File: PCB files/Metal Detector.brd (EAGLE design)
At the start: 100 x 80 mm, 105 parts, among them IC1 NE5534AD, IC2 BQ24133RGYR, IC4 ESP32-WROOM-32UE-N4, IC6 TLV62130ARGTR, IC7 TLV1117-33IDCYR, J1 DG128-7.5, J2 DG128-7.5, Q1 IRF740, Q11 MMBT3904, Q3 SI2312CDS-T1-GE3, Q5 SI2312CDS-T1-GE3, Q6 SI2323CDS-T1-GE3, Q9 MMBT3904, X2 DC21MMX

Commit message: Add files via upload
Started design PCB layout first start from battery charge circut, still desing process
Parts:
- removed Q5: SI2312CDS-T1-GE3, SI2312CDS-T1-GE3:SOT95P237X112-3N
- removed Q6: SI2323CDS-T1-GE3, SI2323CDS-T1-GE3:SOT95P237X112-3N
- removed R30: 0.02RΩ, rcl:R1206
- removed R31: 0RΩ, rcl:R1206
- removed R33: 0.01RΩ, rcl:R1206
- added Q2, Q4: IRF740, IRF740:TO220BV
- added R14: 0.02Ω, rcl:R2010
- added R19: 0.01Ω, rcl:R2010
- added R21: 0Ω, rcl:R0603
- Q3: value SI2312CDS-T1-GE3 -> IRF9630; device SI2312CDS-T1-GE3:SOT95P237X112-3N -> IRF9630:TO254P465X1024X2050-3P
- moved BATTERYPIN 1425.9 mm to (6.35, 58.4), turned to 270 degrees
- moved R49 1362.9 mm to (44.5, 58.4), turned to 270 degrees
- moved R43 671.6 mm to (57.1, 55.9)
- moved R42 670.4 mm to (57.1, 59.7), turned to 180 degrees
- moved R41 666.6 mm to (48.3, 63.5)
- moved C37 665.2 mm to (34.3, 77.5), turned to 180 degrees
- moved C38 662.8 mm to (52.1, 63.5)
- moved C35 639.0 mm to (63.5, 92.7), turned to 90 degrees
- moved R40 625.3 mm to (57.1, 48.3)
- moved R39 621.0 mm to (47.0, 52.1)
- moved R38 617.7 mm to (52.1, 52.1)
- moved R37 607.7 mm to (47.0, 48.3)
- moved R35 607.3 mm to (62.2, 64.8)
- moved R36 604.4 mm to (52.1, 48.3)
- moved C34 603.8 mm to (66.0, 64.8), turned to 180 degrees
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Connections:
- net 12V_IN: now also Q2.D; no longer Q3.3
- net ACN: now also R21.2; no longer R31.1
- net ACP: now also Q4.D, R14.1; no longer Q5.3, R30.1
- net GND: now also BATTERYPIN.2, BATTERYPIN.4; no longer BATTERYPIN.1, BATTERYPIN.3
- net N$21: now also Q2.S, Q4.S; no longer Q3.2, Q5.2
- net N$22: now also Q2.G, Q4.G; no longer Q3.1, Q5.1
- net N$23: now also Q3.1; no longer Q6.1
- net SRP: now also R19.1; no longer R33.1
- net TS: now also BATTERYPIN.3; no longer BATTERYPIN.2
- net VBATT: now also BATTERYPIN.1, Q3.2, R19.2; no longer BATTERYPIN.4, Q6.3, R33.2
- net VCCINT: now also Q3.3, R14.2, R21.1; no longer Q6.2, R30.2, R31.2
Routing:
- net VBATT: track 0.00 -> 55.2 mm
- net 12V_IN: track 0.00 -> 37.4 mm
- net N$22: track 0.00 -> 28.0 mm
- net N$21: track 0.00 -> 25.4 mm
- net VCCINT: track 0.00 -> 22.5 mm
- net ACP: track 0.00 -> 22.0 mm, vias 0 -> 1
- net VCC: track 0.00 -> 16.9 mm
- net SRP: track 0.00 -> 10.3 mm
- net OVPSET: track 0.00 -> 8.63 mm
- net ACN: track 0.00 -> 7.05 mm, vias 0 -> 1
- net N$16: track 0.00 -> 6.34 mm
- net N$23: track 0.00 -> 5.50 mm
- net AVCC: track 0.00 -> 5.22 mm
- net CMSRC: track 0.00 -> 4.20 mm, vias 0 -> 1
- net TS: track 0.00 -> 3.81 mm
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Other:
- board size 100 x 80 mm -> 89 x 100.3 mm

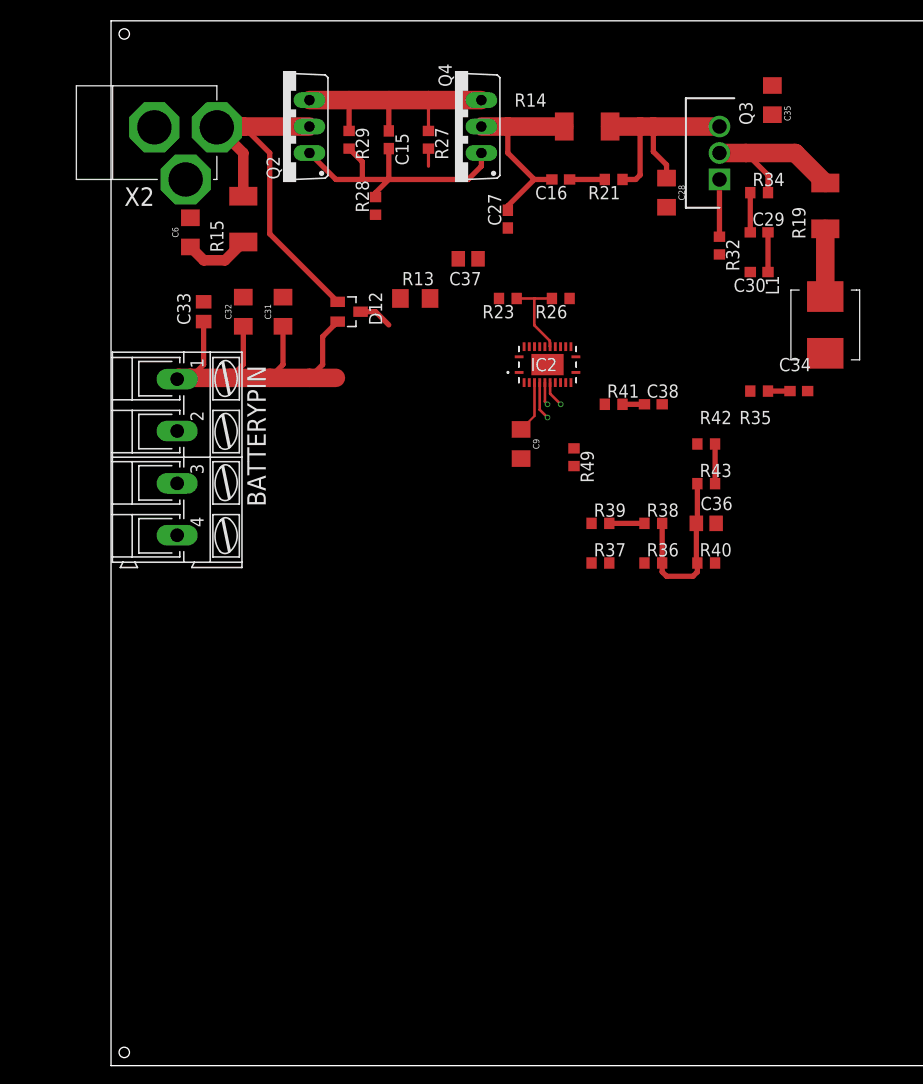
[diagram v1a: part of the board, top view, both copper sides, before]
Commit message: Add files via upload
Battery charge circuit on design progress
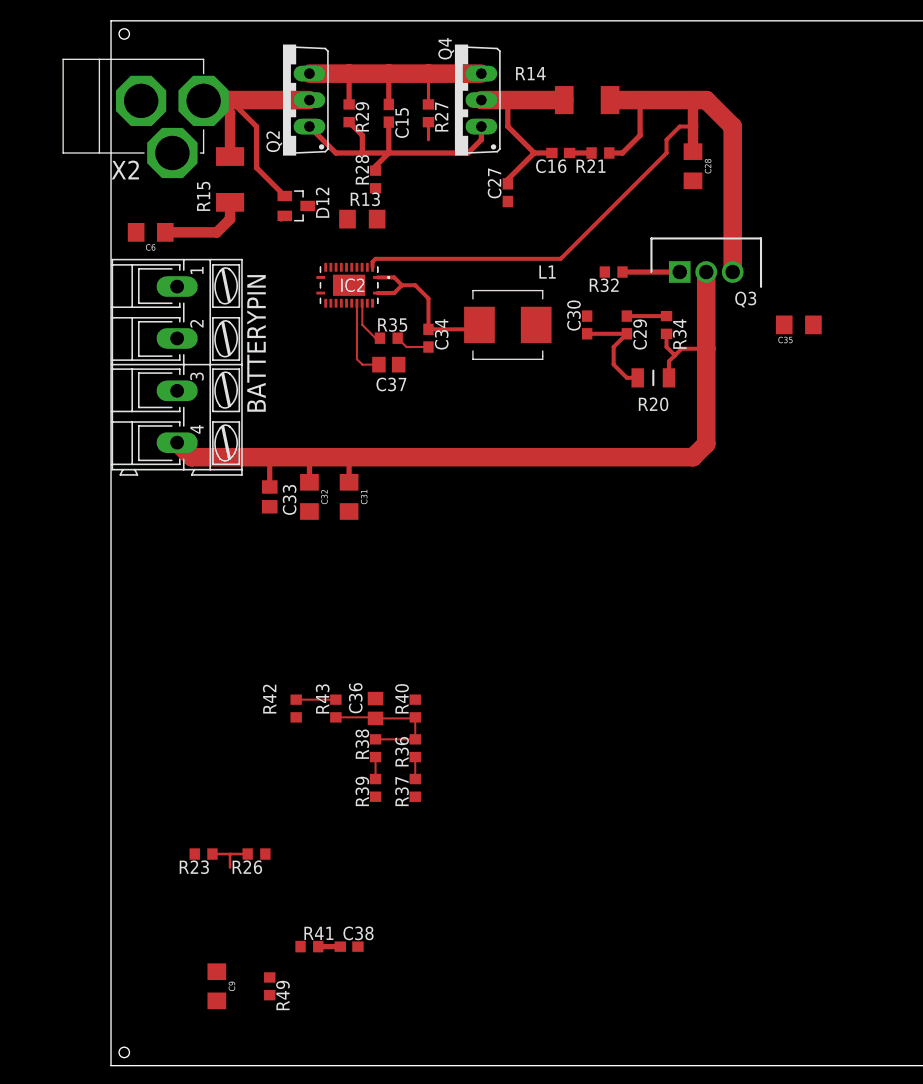
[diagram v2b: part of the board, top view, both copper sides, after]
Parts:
- removed R19: 0.01Ω, rcl:R2010
- added R20: WSL1206R0100FEK18, WSL1206R0100FEK18:RESC3216X89N
- moved R23 60.8 mm to (8.89, 20.3)
- moved R26 60.8 mm to (14.0, 20.3)
- moved C38 59.7 mm to (22.9, 11.4)
- moved C9 59.7 mm to (10.2, 7.62)
- moved R41 59.7 mm to (19.1, 11.4)
- moved R49 58.6 mm to (15.2, 7.62)
- moved R42 46.9 mm to (17.8, 34.3), turned to 270 degrees
- moved R43 41.6 mm to (21.6, 34.3), turned to 90 degrees
- moved C36 36.4 mm to (25.4, 34.3), turned to 270 degrees
- moved C34 35.9 mm to (30.5, 69.8), turned to 270 degrees
- moved R35 35.9 mm to (26.7, 69.8)
- moved R38 34.3 mm to (25.4, 30.5), turned to 90 degrees
- moved R39 33.3 mm to (25.4, 26.7), turned to 90 degrees
- moved R40 31.2 mm to (29.2, 34.3), turned to 90 degrees
- moved L1 30.5 mm to (38.1, 71.1), turned to 0 degrees
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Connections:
- net GND: now also BATTERYPIN.1, BATTERYPIN.3; no longer BATTERYPIN.2, BATTERYPIN.4
- net SRP: now also R20.1; no longer R19.1
- net TS: now also BATTERYPIN.2; no longer BATTERYPIN.3
- net VBATT: now also BATTERYPIN.4, R20.2; no longer BATTERYPIN.1, R19.2
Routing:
- net VCCINT: track 22.5 -> 76.2 mm
- net VBATT: track 55.2 -> 84.6 mm
- net SW: track 0.00 -> 16.4 mm
- net 12V_IN: track 37.4 -> 28.9 mm
- net REGN: track 0.00 -> 7.70 mm
- net AVCC: track 5.22 -> 0.19 mm
- net ACN: track 7.05 -> 2.11 mm, vias 1 -> 0
- net BTST: track 0.00 -> 4.31 mm
- net OVPSET: track 8.63 -> 4.68 mm
- net VCC: track 16.9 -> 13.6 mm
- net N$14: track 3.24 -> 0.00 mm
- net CMSRC: track 4.20 -> 1.69 mm, vias 1 -> 0
- net ACP: track 22.0 -> 19.8 mm, vias 1 -> 0
- net N$16: track 6.34 -> 8.49 mm
- net ISET: track 0.00 -> 2.11 mm
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
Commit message: Add files via upload
Designed Battery charge circut next design power circut and connection two circuit
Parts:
- moved C9 72.4 mm to (27.9, 77.9), turned to 180 degrees
- moved R23 58.8 mm to (15.2, 78.7), turned to 90 degrees
- moved R26 58.5 mm to (17.8, 78.7), turned to 270 degrees
- moved R41 57.3 mm to (15.2, 68.6), turned to 270 degrees
- moved C38 53.9 mm to (15.2, 64.8), turned to 270 degrees
- moved R37 42.6 mm to (21.6, 68.6)
- moved R36 39.4 mm to (19.1, 68.6)
- moved C36 38.3 mm to (21.6, 72.4)
- moved R43 38.3 mm to (17.8, 72.4)
- moved R42 38.2 mm to (15.2, 72.4)
- moved R39 38.1 mm to (24.4, 64.8)
- moved R38 34.5 mm to (21.6, 64.8), turned to 270 degrees
- moved R40 32.1 mm to (19.1, 64.8)
- moved C30 16.5 mm to (31.2, 63.1), turned to 0 degrees
- moved C29 14.9 mm to (36.3, 64.3), turned to 180 degrees
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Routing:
- net BATDRV: track 0.00 -> 35.2 mm, vias 0 -> 2
- net 12V_IN: track 28.9 -> 55.5 mm
- net SRP: track 10.1 -> 36.3 mm, vias 0 -> 2
- net TS: track 3.81 -> 28.0 mm
- net OVPSET: track 4.68 -> 28.4 mm, vias 0 -> 2
- net VBATT: track 84.6 -> 107.4 mm
- net ACP: track 19.8 -> 40.9 mm, vias 0 -> 2
- net SRN: track 3.81 -> 22.9 mm, vias 0 -> 2
- net TTC: track 0.00 -> 17.6 mm
- net CMSRC: track 1.69 -> 19.2 mm, vias 0 -> 2
- net AVCC: track 0.19 -> 16.6 mm
- net ACDRV: track 0.00 -> 12.7 mm, vias 0 -> 2
- net ACN: track 2.11 -> 13.5 mm, vias 0 -> 2
- net VCC: track 13.6 -> 24.9 mm
- net CELL: track 0.00 -> 9.29 mm
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- added copper zone on layer 1, net VBATT

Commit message: Add files via upload
Removed all component ot board
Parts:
- removed R14: 0.02Ω, rcl:R2010
- removed R3, R8: 10kΩ, rcl:0207/10
- removed R4: 2.2kΩ, rcl:0207/10
- added R19: 20Ω, rcl:R1206
- added R30, R31: 10KΩ, rcl:R1206
- added R33: 2.2kΩ, rcl:R1206
- R1: value 20Ω -> WSL1206R0200FEK18; device rcl:0207/10 -> WSL1206R0100FEK18:RESC3216X89N
- moved ENCODER 1384.2 mm to (50.8, 41.9)
- moved SERIAL 1365.0 mm to (27.9, 10.2)
- moved DISPLAY 1348.3 mm to (39.4, 26.7)
- moved IC7 1330.5 mm to (66.0, 67.3)
- moved R46 1327.9 mm to (58.4, 25.4)
- moved R48 1323.8 mm to (36.8, 44.5)
- moved Q11 1317.1 mm to (57.1, 20.3)
- moved HEADPHONE 1314.3 mm to (47.0, 10.2)
- moved D5 1314.0 mm to (81.3, 39.4)
- moved C24 1312.8 mm to (68.6, 39.4)
- moved C23 1312.5 mm to (74.9, 39.4)
- moved Q9 1310.9 mm to (62.2, 20.3)
- moved SPEAKER 1308.0 mm to (11.4, 8.89)
- moved R44 1305.4 mm to (82.5, 44.5), turned to 90 degrees
- moved R25 1298.3 mm to (78.7, 44.5), turned to 90 degrees
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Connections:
- net ACP: now also R1.1; no longer R14.1
- net GND: now also R30.1; no longer R3.2
- net IO27: now also R33.2; no longer R4.2
- net N$1: now also R31.2; no longer R8.1
- net N$2: now also R19.2; no longer R1.2
- net N$3: now also R19.1, R30.2; no longer R1.1, R3.1
- net N$5: now also R33.1; no longer R4.1
- net N$7: now also R31.1; no longer R8.2
- net VCCINT: now also R1.2; no longer R14.2
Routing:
- net N$7: track 0.00 -> 52.2 mm
- net VCC: track 24.9 -> 55.1 mm
- net VCCINT: track 75.3 -> 96.3 mm
- net N$6: track 0.00 -> 10.2 mm
- net VBATT: track 107.4 -> 114.7 mm
- net N$4: track 0.00 -> 6.35 mm
- net N$1: track 0.00 -> 6.20 mm
- net N$23: track 12.4 -> 10.4 mm
- net ACP: track 40.9 -> 42.8 mm
- removed copper zone on layer 1, net VBATT
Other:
- board size 89 x 100.3 mm -> 85.1 x 100.3 mm

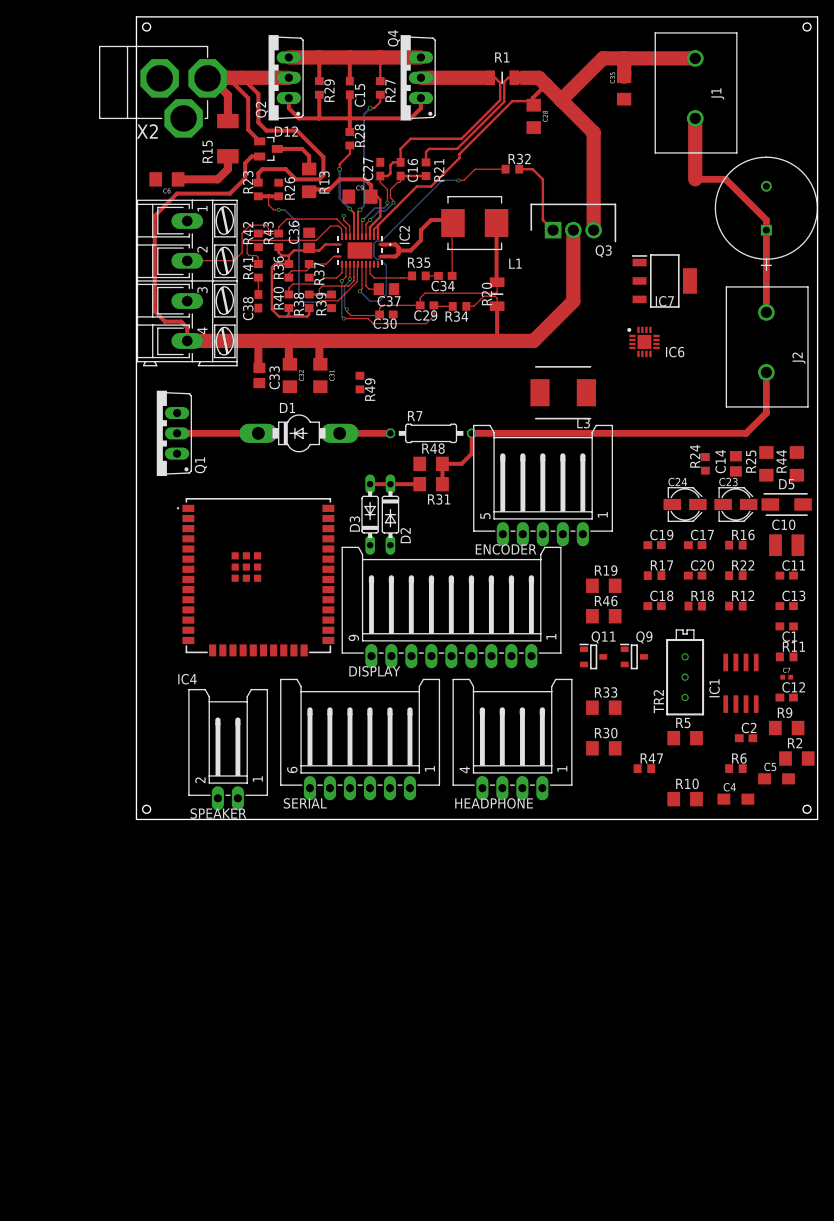
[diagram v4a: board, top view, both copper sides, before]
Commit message: Add files via upload
Optimizated PCB trace and designed 12V to 5V Buck coneventer
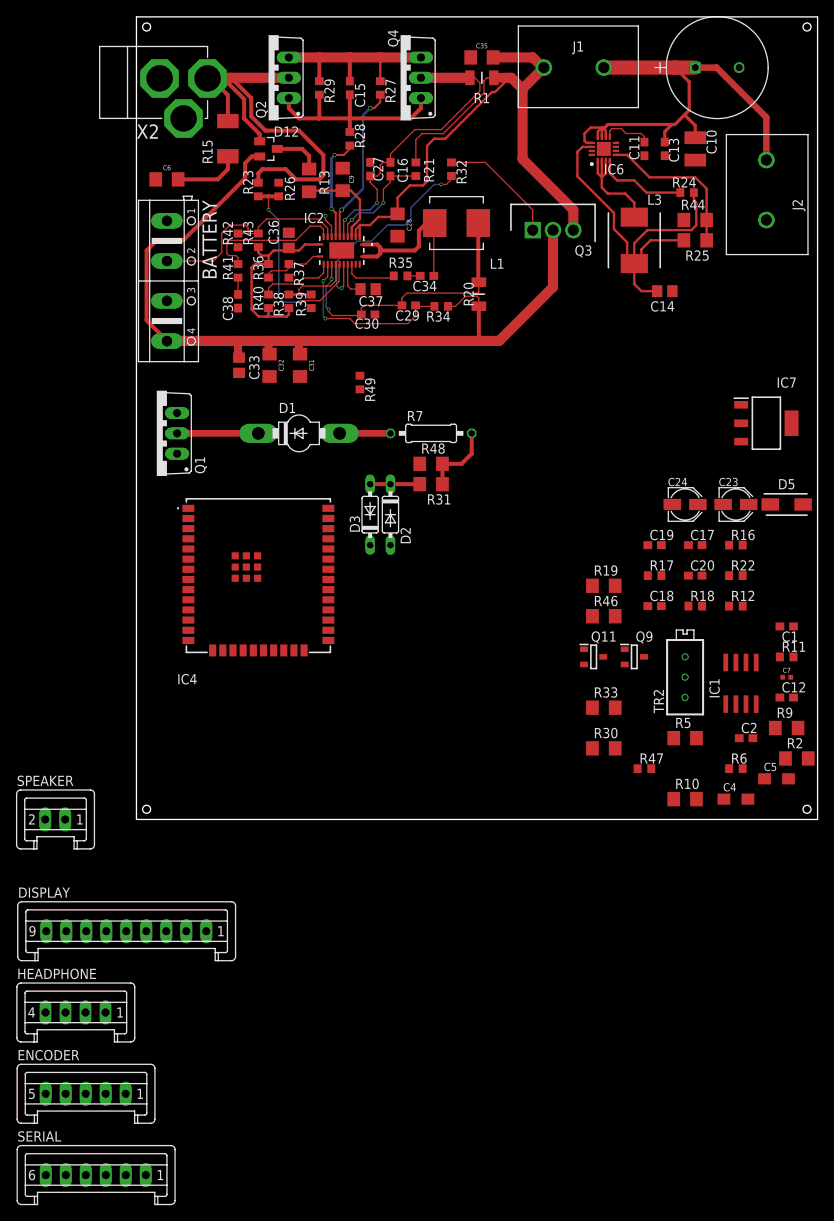
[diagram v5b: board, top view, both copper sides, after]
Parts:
- removed BATTERYPIN: (no value), con-ptr500:AK300/4
- added BATTERY: (no value), con-ptr500:AK500/4
- DISPLAY: device con-amp-mt:L09P -> con-amp-mt:S09P
- ENCODER: device con-amp-mt:L05P -> con-amp-mt:S05P
- HEADPHONE: device con-amp-mt:L04P -> con-amp-mt:S04P
- SERIAL: device con-amp-mt:L06P -> con-amp-mt:S06P
- SPEAKER: device con-amp-mt:L02P -> con-amp-mt:S02P
- moved ENCODER 95.2 mm to (-6.35, -34.3)
- moved HEADPHONE 64.5 mm to (-7.62, -24.1)
- moved SERIAL 63.8 mm to (-5.08, -44.5)
- moved C13 59.1 mm to (66.0, 83.8), turned to 270 degrees
- moved DISPLAY 57.5 mm to (-1.27, -14.0)
- moved C11 56.2 mm to (63.5, 83.8), turned to 270 degrees
- moved C10 50.8 mm to (69.8, 83.8), turned to 270 degrees
- moved R24 34.0 mm to (68.8, 78.4), turned to 0 degrees
- moved R44 33.0 mm to (69.8, 74.9), turned to 180 degrees
- moved R25 29.3 mm to (69.8, 72.4), turned to 0 degrees
- moved IC6 24.7 mm to (58.4, 83.8), turned to 90 degrees
- moved C14 23.3 mm to (66.0, 66.0), turned to 180 degrees
- moved SPEAKER 23.3 mm to (-10.2, 0.00)
- moved C3 22.2 mm to (69.8, 94.0), turned to 0 degrees
- moved IC7 21.8 mm to (78.7, 49.5)
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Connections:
- net GND: now also BATTERY.1, BATTERY.3; no longer BATTERYPIN.1, BATTERYPIN.3
- net TS: now also BATTERY.2; no longer BATTERYPIN.2
- net VBATT: now also BATTERY.4; no longer BATTERYPIN.4
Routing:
- net VCC: track 55.1 -> 135.5 mm
- net N$7: track 52.2 -> 9.26 mm
- net N$30: track 0.00 -> 19.6 mm
- net N$49: track 0.00 -> 14.5 mm
- net VCCINT: track 96.3 -> 84.7 mm
- net N$28: track 0.00 -> 11.4 mm
- net BATDRV: track 35.1 -> 26.7 mm
- net VBATT: track 114.7 -> 106.5 mm
- net N$19: track 0.00 -> 6.31 mm
- net N$23: track 10.4 -> 15.2 mm
- net AVCC: track 16.6 -> 11.9 mm
- net ACP: track 42.8 -> 38.8 mm
- net OVPSET: track 28.4 -> 26.8 mm
- net 12V_IN: track 55.5 -> 56.5 mm
- net CMSRC: track 19.2 -> 20.1 mm
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
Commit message: Add files via upload
Redesign 5V buck conventer circuit for implementation problem
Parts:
- removed IC6: TLV62130ARGTR, TLV62130ARGTR:QFN50P300X300X100-17N
- removed J1: DG128-7.5, DG128-7.5-02P-14-00AH:DG1287502P1400AH
- removed L3: IHLP2525CZER220M11, IHLP2525CZER220M11:INDPM6965X300N
- removed R25: 680kΩ, rcl:R1206
- removed R44: 130kΩ, rcl:R1206
- added C21: 5pF, rcl:C0603
- added C22: 3300pF, rcl:C0603
- added C25, C26: 22uF, SparkFun-Capacitors:1206
- added C8: 10uF/25V, rcl:C1210
- added IC3: TPS54228DDAR, TPS54228DDAR:SOIC127P600X170-9N
- added L2: SRP1265A-4R7M, SRP1265A-4R7M:INDM135125X640N
- added ON-OFF: (no value), con-amp-mt:S02P
- added R3: 22.1kΩ, rcl:R0603
- added R4: 124kΩ, rcl:R0603
- C11: value 3300pF -> 0.1uF
- C14: value 22uF/6.3V -> 15pF; device rcl:C0805 -> rcl:C0603
- R24: value 100kΩ -> 10kΩ
- moved C11 170.4 mm to (-12.7, -68.6), turned to 0 degrees
- moved C14 169.3 mm to (-12.7, -83.8), turned to 0 degrees
- moved R24 30.5 mm to (67.6, 47.9)
- moved C10 30.5 mm to (68.6, 53.3)
- moved C13 30.5 mm to (64.8, 53.3)
- moved Q3 12.5 mm to (44.5, 85.1)
- moved C3 11.4 mm to (58.4, 94.0)
- moved J2 10.2 mm to (78.7, 85.1)
- moved R32 1.27 mm to (38.1, 81.3)
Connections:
- removed net N$28: IC6.4, R24.1
- removed net N$49: IC6.1, IC6.2, IC6.3, L3.1
- removed net VCCINT: C28.1, C35.1, IC2.2, IC2.3, J1.2, Q3.3, R1.2, R21.1
- new net N$17: IC3.1, R24.1
- new net N$18: C11.1, IC3.7
- new net N$24: C14.1, IC3.2, R3.2, R4.1
- new net N$33: C22.1, IC3.4
- new net ON-OFF: ON-OFF.1, R24.2
- net GND: now also C21.2, C22.2, C25.2, C26.2, C8.2, IC3.5, IC3.9, R3.1; no longer C11.2, C14.1, IC6.15, IC6.16, IC6.17, IC6.6, IC6.7, IC6.8, R44.2
- net N$19: now also C11.2, IC3.6, L2.1; no longer C11.1, IC6.9
- net N$30: now also C21.1, IC3.3; no longer IC6.5, R25.2, R44.1
- net VCC: now also C25.1, C26.1, C28.1, C35.1, C8.1, IC2.2, IC2.3, IC3.8, L2.2, ON-OFF.2, Q3.3, R1.2, R21.1, R4.2; no longer IC6.10, IC6.11, IC6.12, IC6.13, IC6.14, J1.1, L3.2, R24.2, R25.1
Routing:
- net VCCINT: track 84.7 -> 0.00 mm
- net N$30: track 19.6 -> 0.00 mm
- net N$49: track 14.5 -> 0.00 mm
- net VCC: track 135.5 -> 124.1 mm
- net N$28: track 11.4 -> 0.00 mm
- net VBATT: track 106.5 -> 115.5 mm
- net N$23: track 15.2 -> 7.58 mm
- net N$19: track 6.31 -> 0.00 mm
- net BATDRV: track 26.7 -> 25.6 mm
